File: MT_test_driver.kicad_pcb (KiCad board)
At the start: 2 copper layers, 71.2 x 46.5 mm, 75 parts, among them J1 header_SWD, J2 barreljack_5.5mm, J3 16P_USB_C, J4 header_temp, J5 header_mag, J6 header_battery, SW1 SW_Push, SW2 SW_Push, U1 DRV8871DDA, U2 AMS1117-3.3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

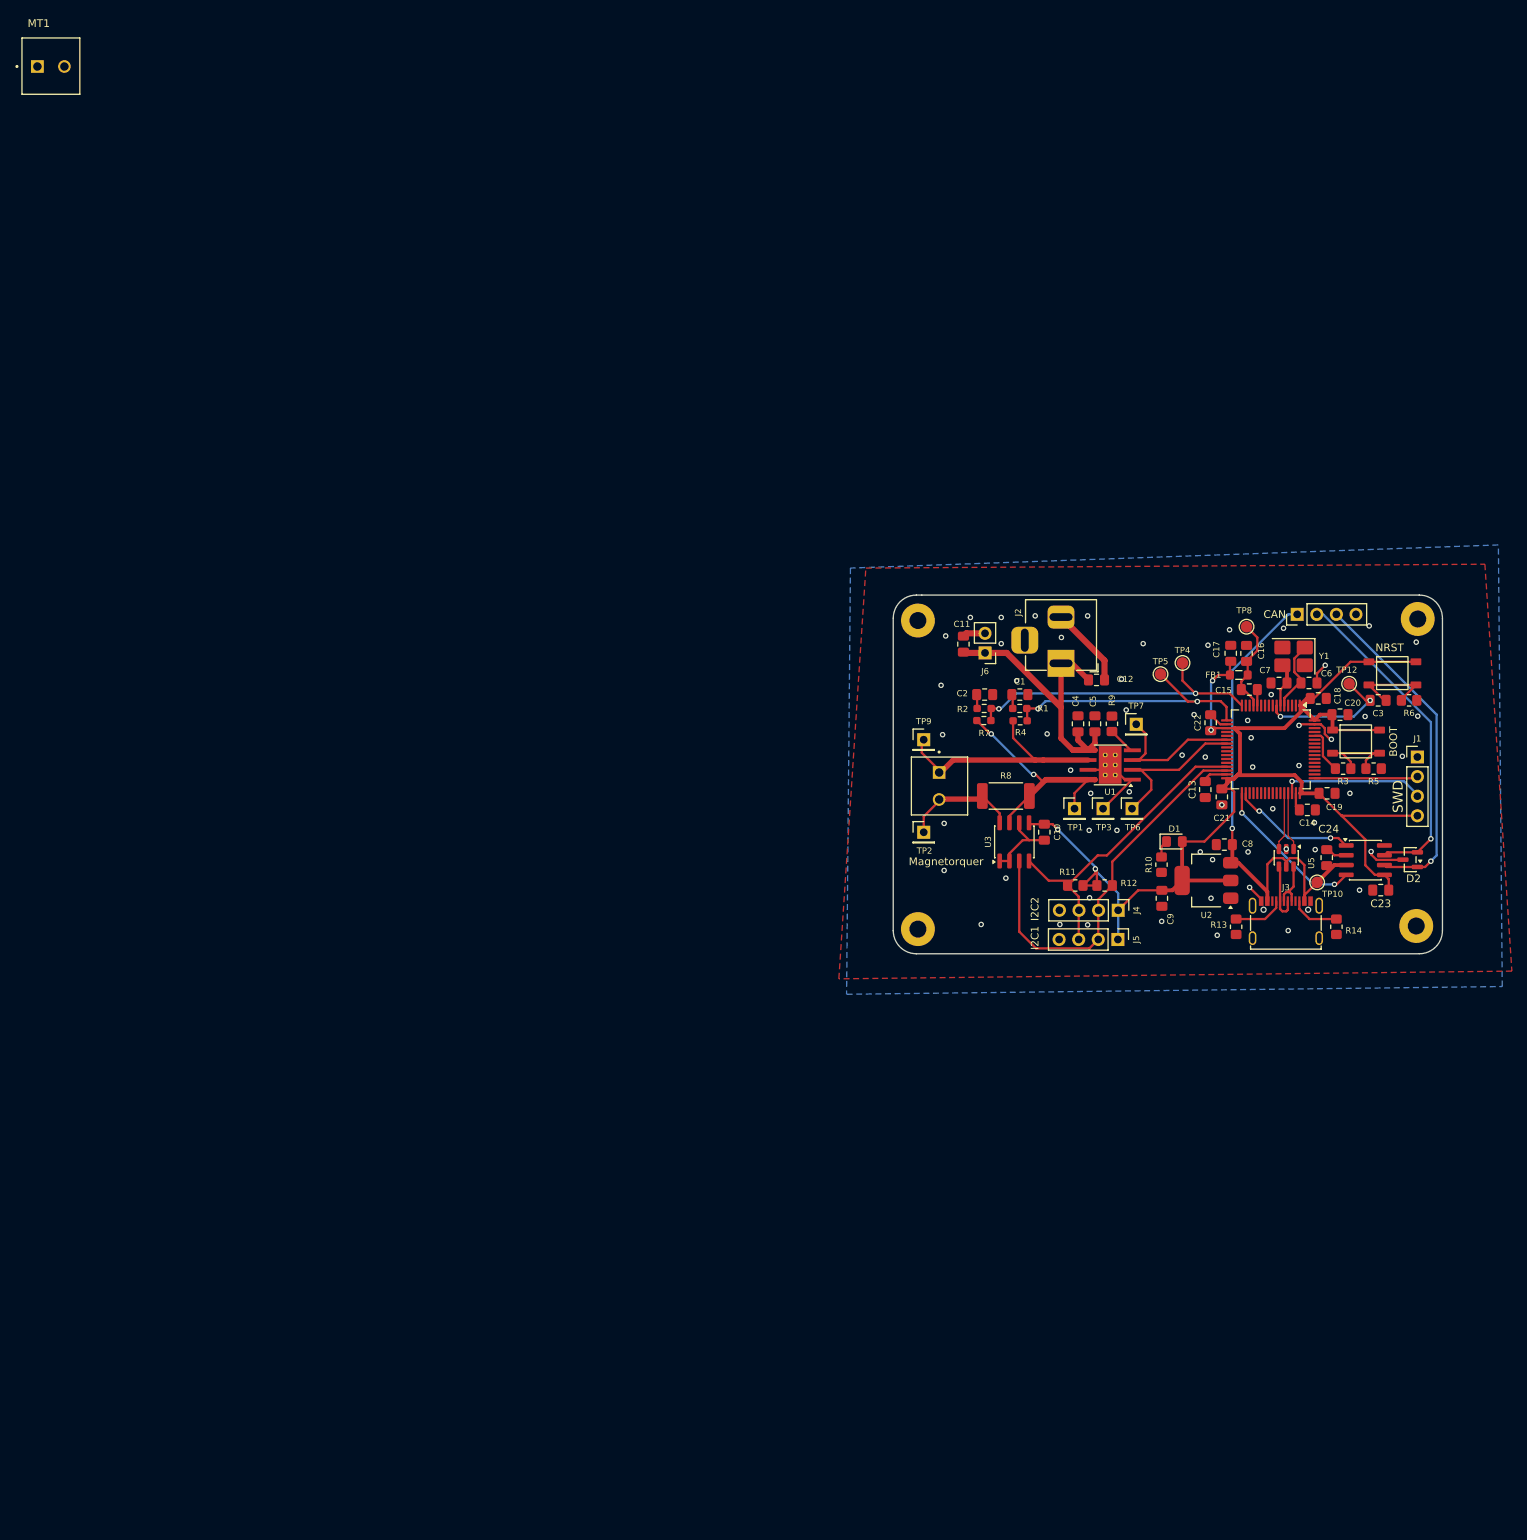
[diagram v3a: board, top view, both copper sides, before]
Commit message: changes in layout , moving components
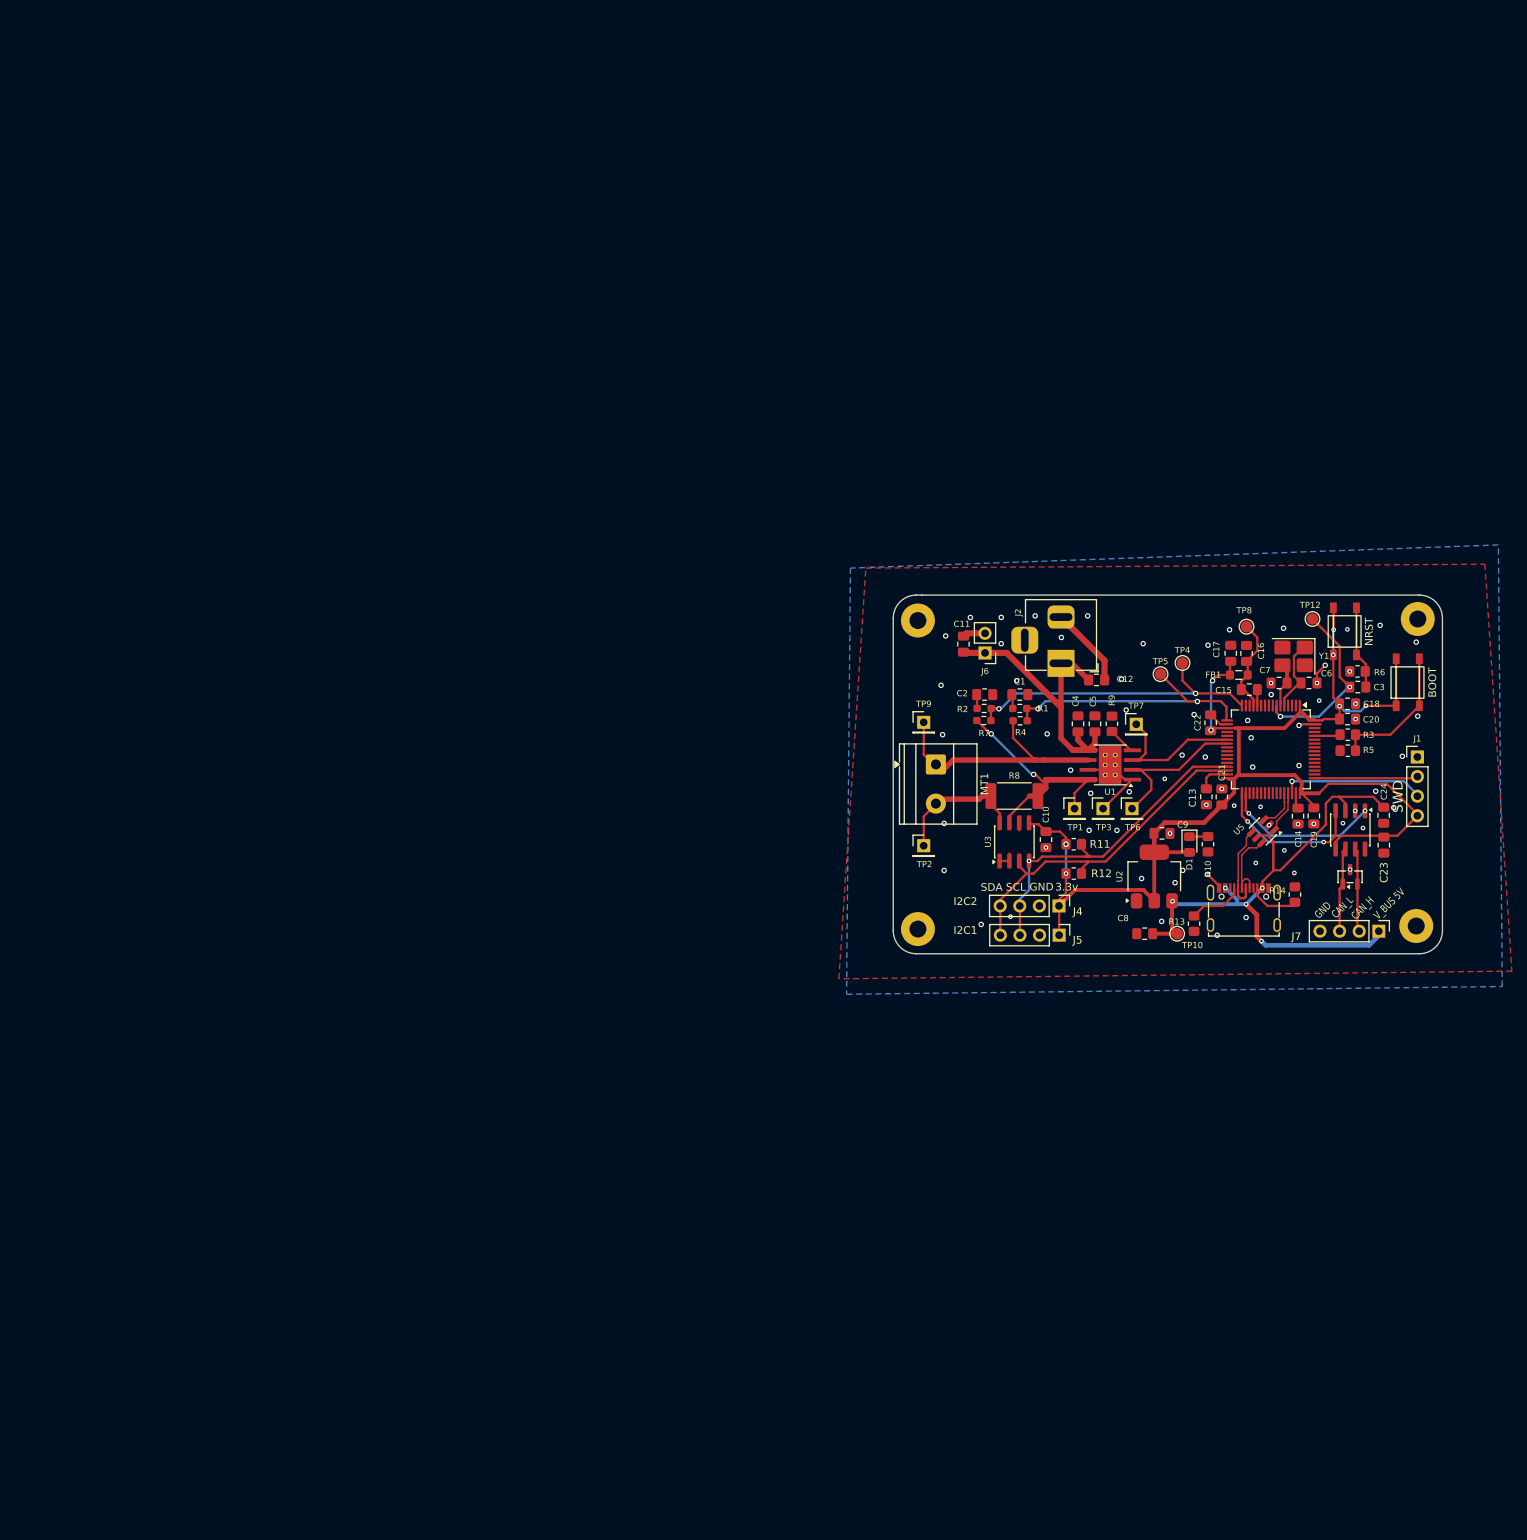
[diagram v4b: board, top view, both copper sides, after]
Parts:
- removed Magnetorquer: Screw_Terminal, Library:screwterminal_PHOENIX_1751248
- MT1: footprint Library:screwterminal_PHOENIX_1751248 -> TerminalBlock_Phoenix:TerminalBlock_Phoenix_MKDS-1,5-2-5.08_1x02_P5.08mm_Horizontal
- moved MT1 146.9 mm to (119.3, 94.5), turned to -90 degrees
- moved J7 42.4 mm to (176.7, 116.1), turned to -90 degrees
- moved TP10 19.3 mm to (150.6, 116.4)
- moved C8 15.5 mm to (146.4, 116.4)
- moved TP12 9.65 mm to (168.2, 75.6)
- moved SW1 9.28 mm to (179.0, 87.6), turned to 90 degrees
- moved C24 9.19 mm to (177.4, 101.0), turned to 90 degrees
- moved C9 8.41 mm to (148.6, 103.4), turned to 0 degrees
- moved D2 8.10 mm to (173.0, 109.0), turned to 90 degrees
- moved J4 7.70 mm to (135.3, 112.8)
- moved R6 7.67 mm to (174.0, 82.4), turned to 0 degrees
- moved J5 7.63 mm to (135.3, 116.6)
- moved R14 6.81 mm to (165.9, 111.3), turned to 90 degrees
- moved U2 6.78 mm to (147.6, 109.0), turned to 90 degrees
- moved R10 6.58 mm to (154.6, 104.8)
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- renumbered CAN to J7
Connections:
- J4 pad 2: /I2C_SDA -> GND
- J4 pad 4: GND -> /I2C_SDA
- J5 pad 2: /I2C_SDA -> GND
- J5 pad 4: GND -> /I2C_SDA
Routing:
- net /CAN_L: track 44.1 -> 11.0 mm, vias 1 -> 0
- net /CAN_H: track 42.6 -> 10.9 mm, vias 1 -> 0
- net GND: track 58.3 -> 41.6 mm, vias 61 -> 73
- net VBUS: track 67.9 -> 81.0 mm, vias 1 -> 5
- net /BOOT0_sw: track 10.9 -> 17.8 mm
- net /I2C_SDA: track 51.4 -> 45.1 mm
- net /NRST: track 18.6 -> 23.8 mm
- net /USBR_D-: track 7.89 -> 11.3 mm
- net /CAN_TX: track 17.0 -> 20.4 mm
- net +3.3V: track 172.8 -> 169.5 mm, vias 4 -> 8
- net /USBR_D+: track 6.61 -> 9.75 mm
- net /BOOT0: track 5.84 -> 3.36 mm
- net Net-(MT1-Pin_2): track 15.2 -> 17.5 mm
- net /USB_D-: track 7.54 -> 5.28 mm
- net /USB_D+: track 7.54 -> 5.57 mm
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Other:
- board text added: "3.3v"
- board text added: "CAN_H"
- board text added: "CAN_L"
- board text added: "GND"
- board text added: "SCL"
- board text added: "SDA"
- board text added: "V_BUS 5V"

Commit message: final changes
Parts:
- moved J3 1.70 mm to (159.3, 115.9)
- moved TP6 1.22 mm to (143.5, 100.2)
- moved TP1 1.20 mm to (138.5, 100.2)
- moved TP10 0.56 mm to (150.0, 116.4)
- moved C12 0.06 mm to (140.1, 83.4)
- renumbered TP12 to TP11
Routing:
- net Net-(U1-OUT2): track 36.8 -> 29.9 mm
- net /USBR_D+: track 9.75 -> 13.0 mm
- net /CC2: track 6.35 -> 8.43 mm
- net GND: track 41.6 -> 43.0 mm, vias 73 -> 75
- net Net-(U1-IN2): track 21.5 -> 22.7 mm
- net /USBR_D-: track 11.3 -> 12.3 mm
- net VBUS: track 81.0 -> 80.3 mm, vias 5 -> 3
- net /CC1: track 7.21 -> 6.64 mm
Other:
- board text added: "3.3V"
- board text added: "SWDCLK"
- board text added: "SWDIO"
- board text removed: "SWD"

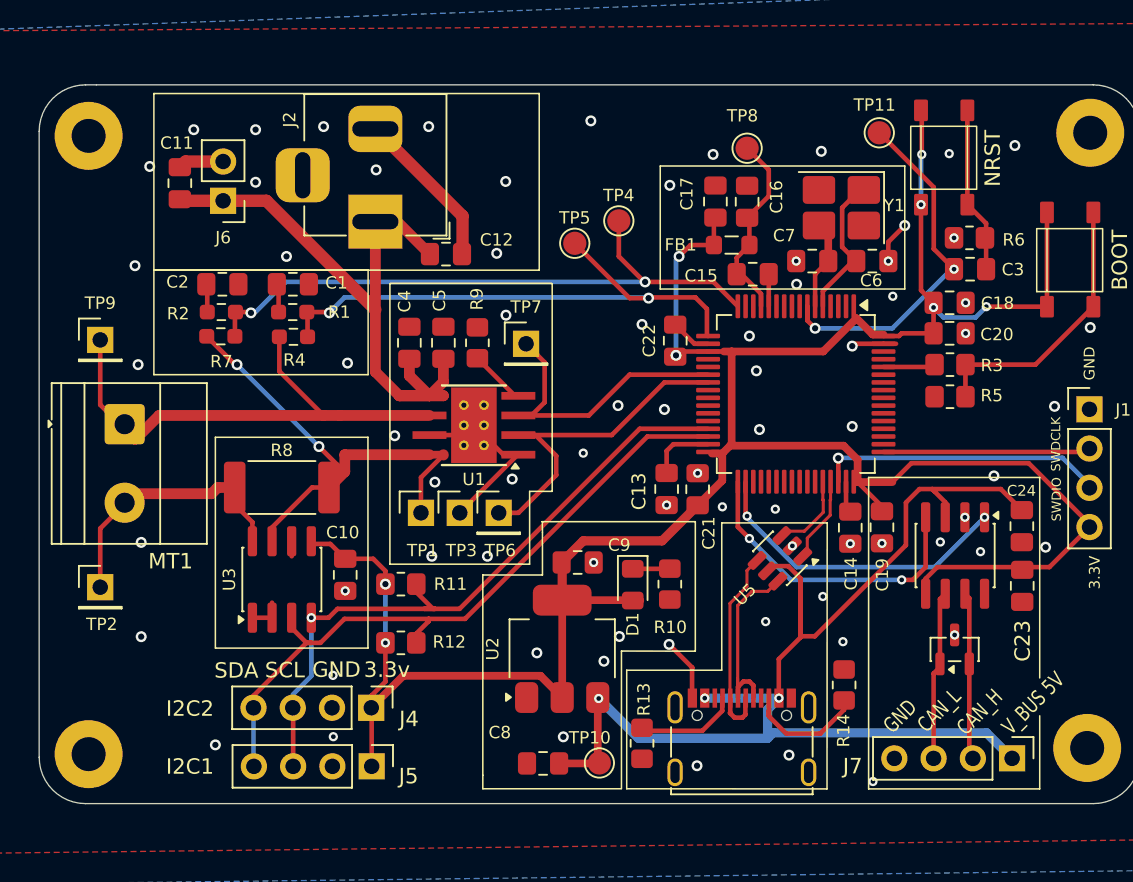
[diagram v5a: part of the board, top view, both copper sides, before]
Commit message: added gpio LED for debugging
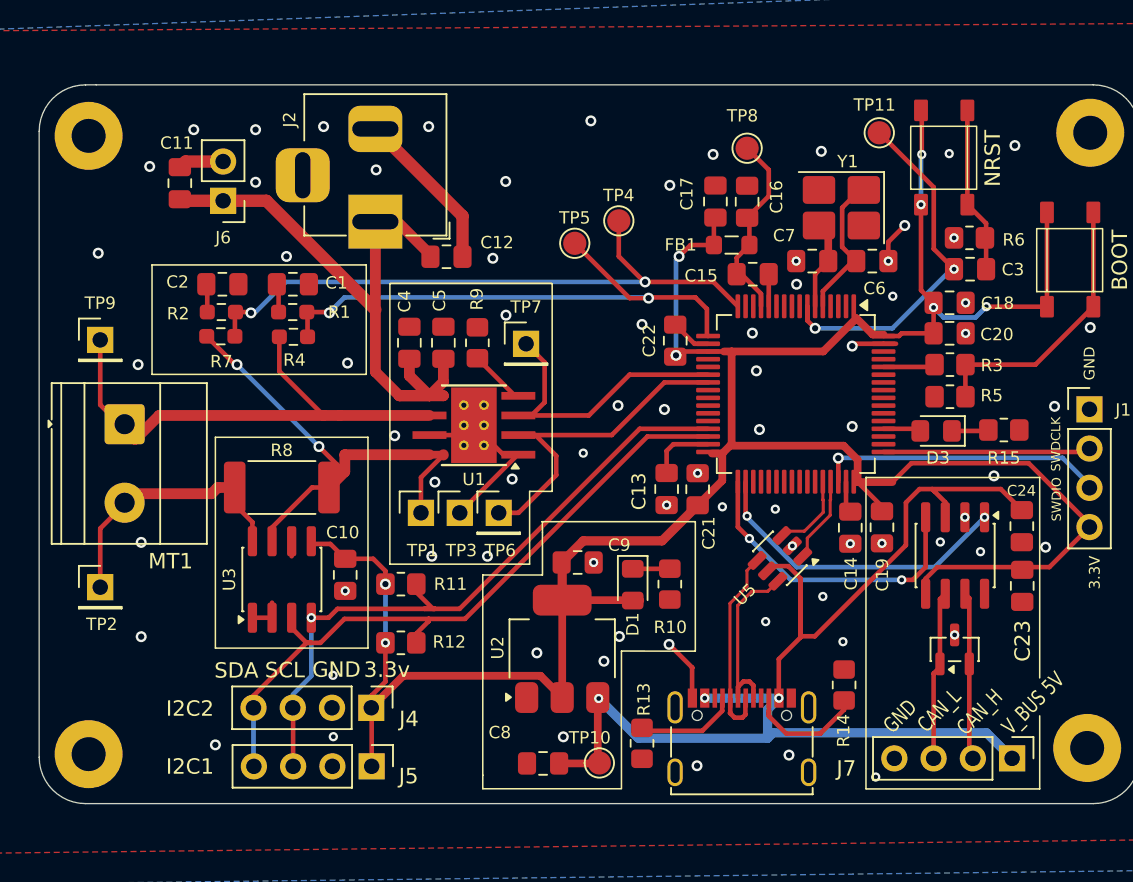
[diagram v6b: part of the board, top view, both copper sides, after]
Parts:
- added D3: LED, LED_SMD:LED_0805_2012Metric_Pad1.15x1.40mm_HandSolder, F.Cu at (171.8, 94.9)
- added R15: 2k2, Resistor_SMD:R_0805_2012Metric_Pad1.20x1.40mm_HandSolder, F.Cu at (176.2, 94.8)
- moved C12 0.17 mm to (140.2, 83.6)
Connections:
- U4 pad 52: unconnected-(U4-PC11-Pad52) -> Net-(D3-A)
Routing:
- net Net-(D3-A): track 0.00 -> 2.44 mm
- net Net-(D3-K): track 0.00 -> 2.38 mm
- net /USBR_D+: track 13.0 -> 12.3 mm
